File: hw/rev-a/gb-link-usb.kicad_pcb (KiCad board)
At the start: 2 copper layers, 34.2 x 62.2 mm, 57 parts, among them J101 TYPE-C-31-M-12, J102 Link cable, SW1 SKRPABE010, SW2 SKRPABE010, U1 RP2350A, U101 USBLC6-2SC6, U102 SN74LVC1T45DBVR, U103 SN74LVC1T45DBVR, U104 SN74LVC1T45DBVR, U105 TPD4E05U06DQAR, U2 NCP1117ST33T3G, U3 W25Q128JVSIQ, X1 ABM8-272-T3

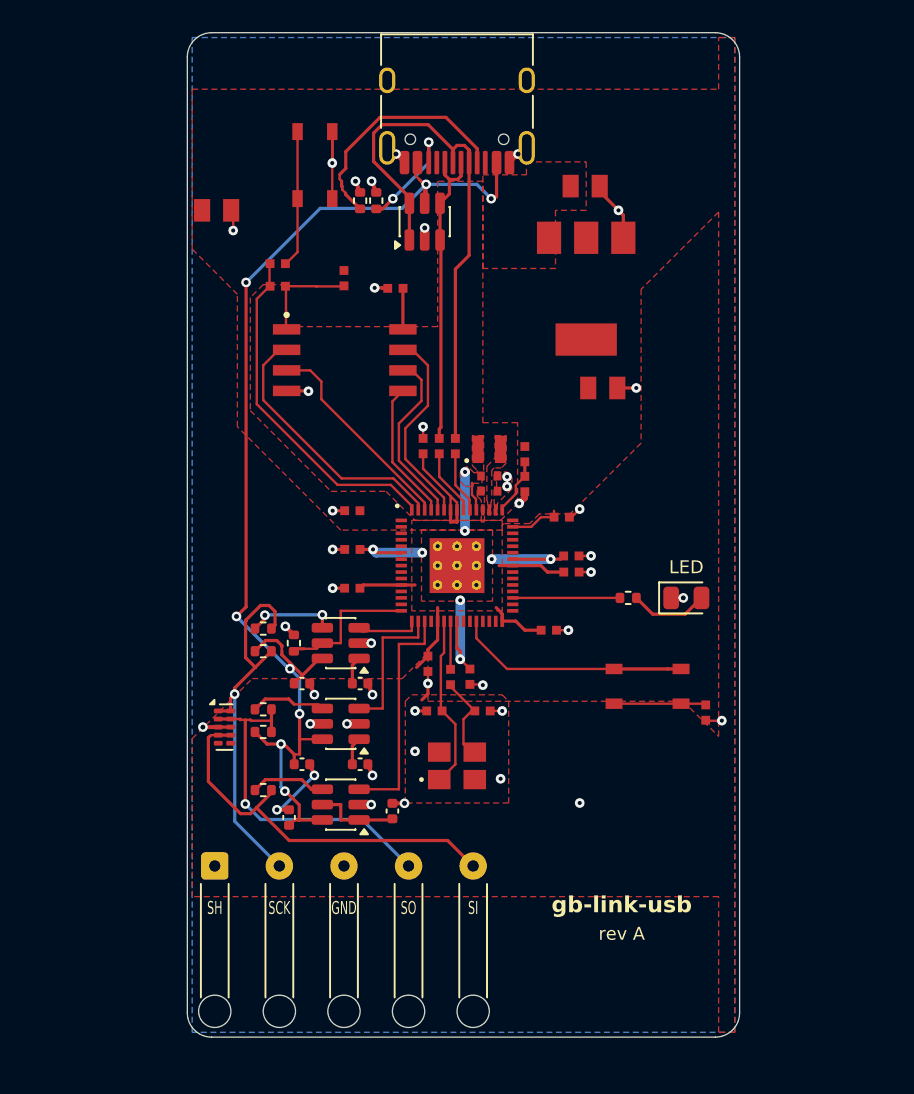
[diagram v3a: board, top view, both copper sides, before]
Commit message: PCB rev A: link simulation -> 220R + 100 pF, routing tidy-up, height check, Gerber render, hw README
Co-Authored-By: Claude Opus 5.5 (1M context) <noreply@anthropic.com>
Claude-Session: https://claude.ai/code/session_01MZ3uQJCcn6FcjzVDhZnLJN
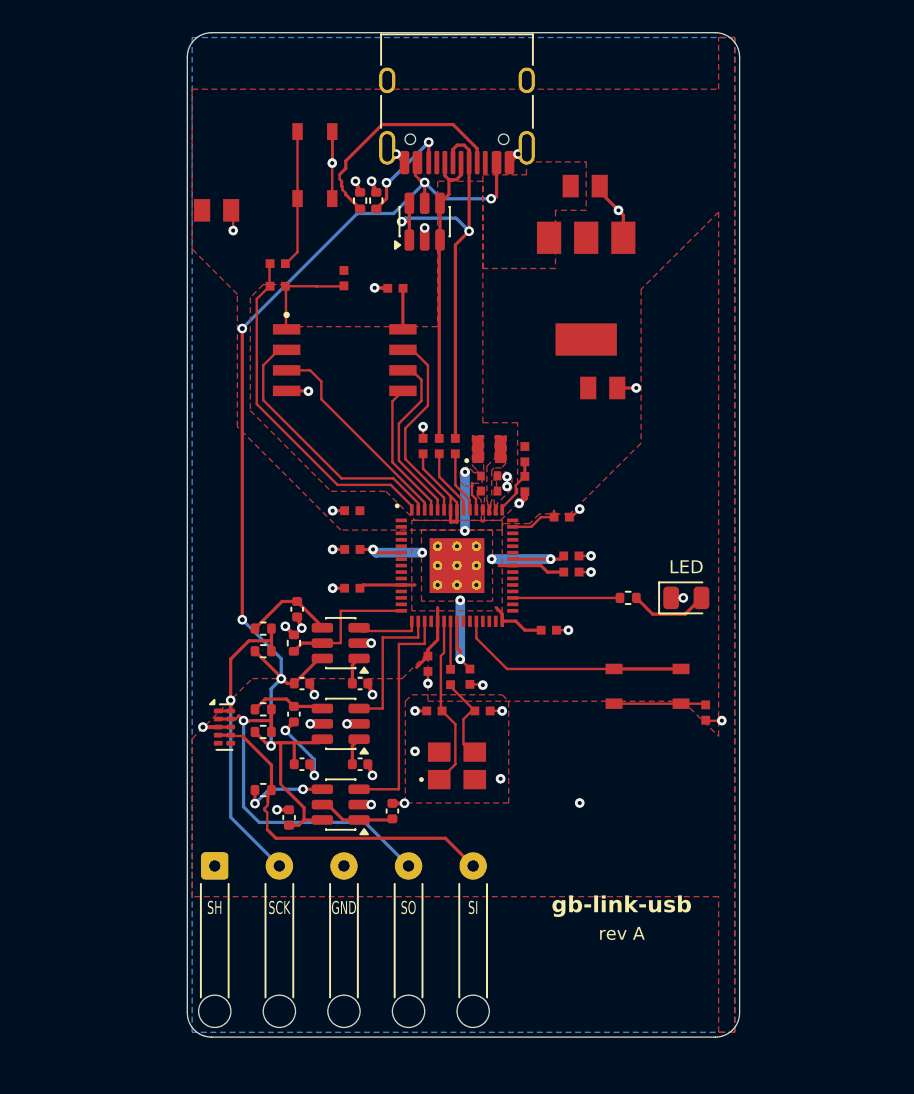
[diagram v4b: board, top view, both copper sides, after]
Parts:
- added C107: 100p, Capacitor_SMD:C_0402_1005Metric, F.Cu at (90.1, 102.7)
- added C108: 100p, Capacitor_SMD:C_0402_1005Metric, F.Cu at (89.9, 109.2)
- R104, R105, R106: value 33 -> 220
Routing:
- net USB_D-: track 33.5 -> 27.6 mm, vias 0 -> 2
- net VBUS: track 75.3 -> 71.0 mm, vias 8 -> 6
- net /Link/LINK_SCK: track 24.0 -> 19.9 mm
- net /Link/LINK_SI: track 24.5 -> 22.0 mm
- net /Link/CC1: track 14.9 -> 14.2 mm
- net /Link/B_SI: track 4.69 -> 5.38 mm, vias 0 -> 2
- net GND: track 44.1 -> 44.8 mm, vias 43 -> 45
- net +3V3: track 37.1 -> 36.6 mm
- net /Link/B_SCK: track 5.46 -> 5.64 mm, vias 2 -> 0

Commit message: PCB rev A: independent review fixes (R106 1k, longer board behind cable holes, USB-C flush, 16 MB flash, docs)
Co-Authored-By: Claude Opus 5.5 (1M context) <noreply@anthropic.com>
Claude-Session: https://claude.ai/code/session_01MZ3uQJCcn6FcjzVDhZnLJN
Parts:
- J101: footprint Connector_USB:USB_C_Receptacle_HRO_TYPE-C-31-M-12 -> gb-link-usb:USB_C_Receptacle_HRO_TYPE-C-31-M-12_Flush
- R106: value 220 -> 1k
- moved J101 0.35 mm to (100.0, 70.7)
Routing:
- net /Link/B_SI: track 5.38 -> 19.4 mm
- net USB_D-: track 27.6 -> 37.2 mm
- net +3V3: track 36.6 -> 44.6 mm, vias 0 -> 2
- net VBUS: track 71.0 -> 76.1 mm, vias 6 -> 8
- net /Link/CC2: track 6.80 -> 4.98 mm, vias 2 -> 0
- net GND: track 44.8 -> 43.1 mm
- net /Link/LINK_SCK: track 19.9 -> 21.0 mm
- net /Link/LINK_SI: track 22.0 -> 22.6 mm, vias 0 -> 1
- net /Link/LINK_SO: track 22.0 -> 21.5 mm
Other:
- board size 34.2 x 62.2 mm -> 34.2 x 63.7 mm
